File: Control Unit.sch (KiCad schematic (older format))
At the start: 0 parts

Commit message: made the CU , need to change the IR
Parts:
- added R8: 1K, Resistor_THT:R_Axial_DIN0204_L3.6mm_D1.6mm_P7.62mm_Horizontal, symbol 16bitCpu-rescue:R-Device
- added SW3: SW_Push-Switch, Button_Switch_THT:SW_PUSH-12mm, symbol 16bitCpu-rescue:SW_Push-Switch
- added U58: 7400, Package_DIP:DIP-14_W7.62mm, symbol 74xx:7400
- added U62: 74LS161-74xx, Package_DIP:DIP-16_W7.62mm, symbol 16bitCpu-rescue:74LS161-74xx
- added U63, U64, U65: AT28C64B-15PU, ROM:ZIF-AT28C64B-15PU, symbol AT28C64B-15PU:AT28C64B-15PU
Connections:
- net labels added: +5V-power, ALU_SU, CF, CLR, GND-power, PC_CE, RESET_COUNTER, VCC-power, ZF, ~ALU_EO, ~ALU_FI, ~CLR, ~IR_13AO, ~IR_AI, ~IR_AO, ~PC_CO, ~PC_J, ~R1_AI, ~R1_AO, ~R2_AI, ~R2_AO, ~RAM_AI, ~RAM_AO, ~RAM_MEMOE, ~RAM_MEMWE
- net labels removed: Bus0, Bus1, Bus10, Bus11, Bus12, Bus13, Bus14, Bus15, Bus2, Bus3, Bus4, Bus5, Bus6, Bus7, Bus8, Bus9
- wire segments 25 -> 165
- no-connect marks 0 -> 11

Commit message: non floating ram and ir , added stack register
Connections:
- net ~SI: now reaches U63.13 (I/O2)
- net ~SO: now reaches U63.15 (I/O3)
- no-connect marks 11 -> 9
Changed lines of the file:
@@
 $Descr A2 23386 16535
 encoding utf-8
-Sheet 9 9
+Sheet 9 10
 Title ""
 Date ""
@@
 Wire Wire Line
 	7100 7500 8400 7500
-Wire Wire Line
-	7100 7700 8400 7700
-Wire Wire Line
-	7100 7800 8400 7800
 Wire Wire Line
 	7100 7900 8400 7900
@@
 Text HLabel 8400 7500 2    50   Output ~ 0
 ~PC_CO
-NoConn ~ 8400 7700
-NoConn ~ 8400 7800
 NoConn ~ 8400 7900
 NoConn ~ 8400 8000
@@
 Wire Wire Line
 	7950 1950 7950 3900
+Wire Wire Line
+	7100 7700 9300 7700
+Text HLabel 9300 7700 2    50   Output ~ 0
+~SI
+Wire Wire Line
+	7100 7800 9200 7800
+Text HLabel 9200 7800 2    50   Output ~ 0
+~SO
 $EndSCHEMATC

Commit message: Added X register
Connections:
- net ~XI: now reaches U63.16 (I/O4)
- net ~XO: now reaches U63.17 (I/O5)
- no-connect marks 9 -> 7
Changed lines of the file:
@@
 $Descr A2 23386 16535
 encoding utf-8
-Sheet 9 10
+Sheet 9 11
 Title ""
 Date ""
@@
 Wire Wire Line
 	7100 7500 8400 7500
-Wire Wire Line
-	7100 7900 8400 7900
-Wire Wire Line
-	7100 8000 8400 8000
 Wire Wire Line
 	7100 8100 8400 8100
@@
 Text HLabel 8400 7500 2    50   Output ~ 0
 ~PC_CO
-NoConn ~ 8400 7900
-NoConn ~ 8400 8000
 NoConn ~ 8400 8100
 NoConn ~ 8400 8200
@@
 Text HLabel 9200 7800 2    50   Output ~ 0
 ~SO
+Text HLabel 10600 7900 2    50   Output ~ 0
+~XI
+Text HLabel 10500 8000 2    50   Output ~ 0
+~XO
+Wire Wire Line
+	7100 7900 10600 7900
+Wire Wire Line
+	7100 8000 10500 8000
 $EndSCHEMATC

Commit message: back to 13 bit addresses
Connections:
- net ~IR_13AO renamed ~IR_8O
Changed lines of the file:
@@
 ~IR_AO
 Text HLabel 8450 5750 2    50   Output ~ 0
-~IR_13AO
+~IR_8O
 Text HLabel 8450 5850 2    50   Output ~ 0
 ~PC_J

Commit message: Let there be light
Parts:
- added D100, D101, D102, D103, D104, D105, D106, D107, D108, D109, D110, D111, D112, D113, D114, D115, D116, D117, D118, D97, D98, D99: LED, LED_THT:LED_D3.0mm, symbol Device:LED
- added R105, R106, R107, R108, R109, R110, R111, R112, R113, R114, R115, R116, R117, R118, R119, R120, R121, R122, R123, R124, R125, R126: 220, Resistor_THT:R_Axial_DIN0204_L3.6mm_D1.6mm_P7.62mm_Horizontal, symbol Device:R
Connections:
- net ALU_SU: now also D98.2 (A)
- net GND: now also R105.2, R106.2, R107.2, R108.2, R109.2, R110.2, R111.2, R112.2, R113.2, R114.2, R115.2, R116.2, R117.2, R118.2, R119.2, R120.2, R121.2, R122.2, R123.2, R124.2, R125.2, R126.2
- net PC_CE: now also D112.2 (A)
- net RESET_COUNTER: now also D114.2 (A)
- net ~ALU_EO: now also D99.2 (A)
- net ~ALU_FI: now also D97.2 (A)
- net ~IR_8O: now also D110.2 (A)
- net ~IR_AI: now also D108.2 (A)
- net ~IR_AO: now also D109.2 (A)
- net ~PC_CO: now also D113.2 (A)
- net ~PC_J: now also D111.2 (A)
- net ~R1_AI: now also D100.2 (A)
- net ~R1_AO: now also D101.2 (A)
- net ~R2_AI: now also D102.2 (A)
- net ~R2_AO: now also D103.2 (A)
- net ~RAM_AI: now also D104.2 (A)
- net ~RAM_AO: now also D105.2 (A)
- net ~RAM_MEMOE: now also D106.2 (A)
- net ~RAM_MEMWE: now also D107.2 (A)
- net ~SI: now also D115.2 (A)
- net ~SO: now also D116.2 (A)
- net ~XI: now also D117.2 (A)
- net ~XO: now also D118.2 (A)
- new net: D112.1 (K), R120.1
- new net: D111.1 (K), R119.1
- new net: D110.1 (K), R118.1
- new net: D109.1 (K), R117.1
- new net: D108.1 (K), R116.1
- new net: D107.1 (K), R115.1
- new net: D106.1 (K), R114.1
- new net: D105.1 (K), R113.1
- new net: D104.1 (K), R112.1
- new net: D103.1 (K), R111.1
- new net: D102.1 (K), R110.1
- new net: D101.1 (K), R109.1
- new net: D100.1 (K), R108.1
- new net: D99.1 (K), R107.1
- new net: D98.1 (K), R106.1
- new net: D97.1 (K), R105.1
- new net: D118.1 (K), R126.1
- new net: D117.1 (K), R125.1
- new net: D116.1 (K), R124.1
- new net: D115.1 (K), R123.1
- new net: D114.1 (K), R122.1
- new net: D113.1 (K), R121.1

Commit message: Added NAND GATES in ALU
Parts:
- renumbered D97 to D49, D98 to D50, D99 to D51, D100 to D52, D101 to D53, D102 to D54, D103 to D55, D104 to D56, D105 to D57, D106 to D58, D107 to D59, D108 to D60, D109 to D61, D110 to D62, D111 to D63, D112 to D64, D113 to D65, D114 to D66, D115 to D67, D116 to D68, D117 to D69, D118 to D70, R8 to R49, R105 to R50, R106 to R51, R107 to R52, R108 to R53, R109 to R54, R110 to R55, R111 to R56, R112 to R57, R113 to R58, R114 to R59, R115 to R60, R116 to R61, R117 to R62, R118 to R63, R119 to R64, R120 to R65, R121 to R66, R122 to R67, R123 to R68, R124 to R69, R125 to R70, R126 to R71, SW3 to SW1, U58 to U19, U62 to U20, U63 to U21, U64 to U22, U65 to U23

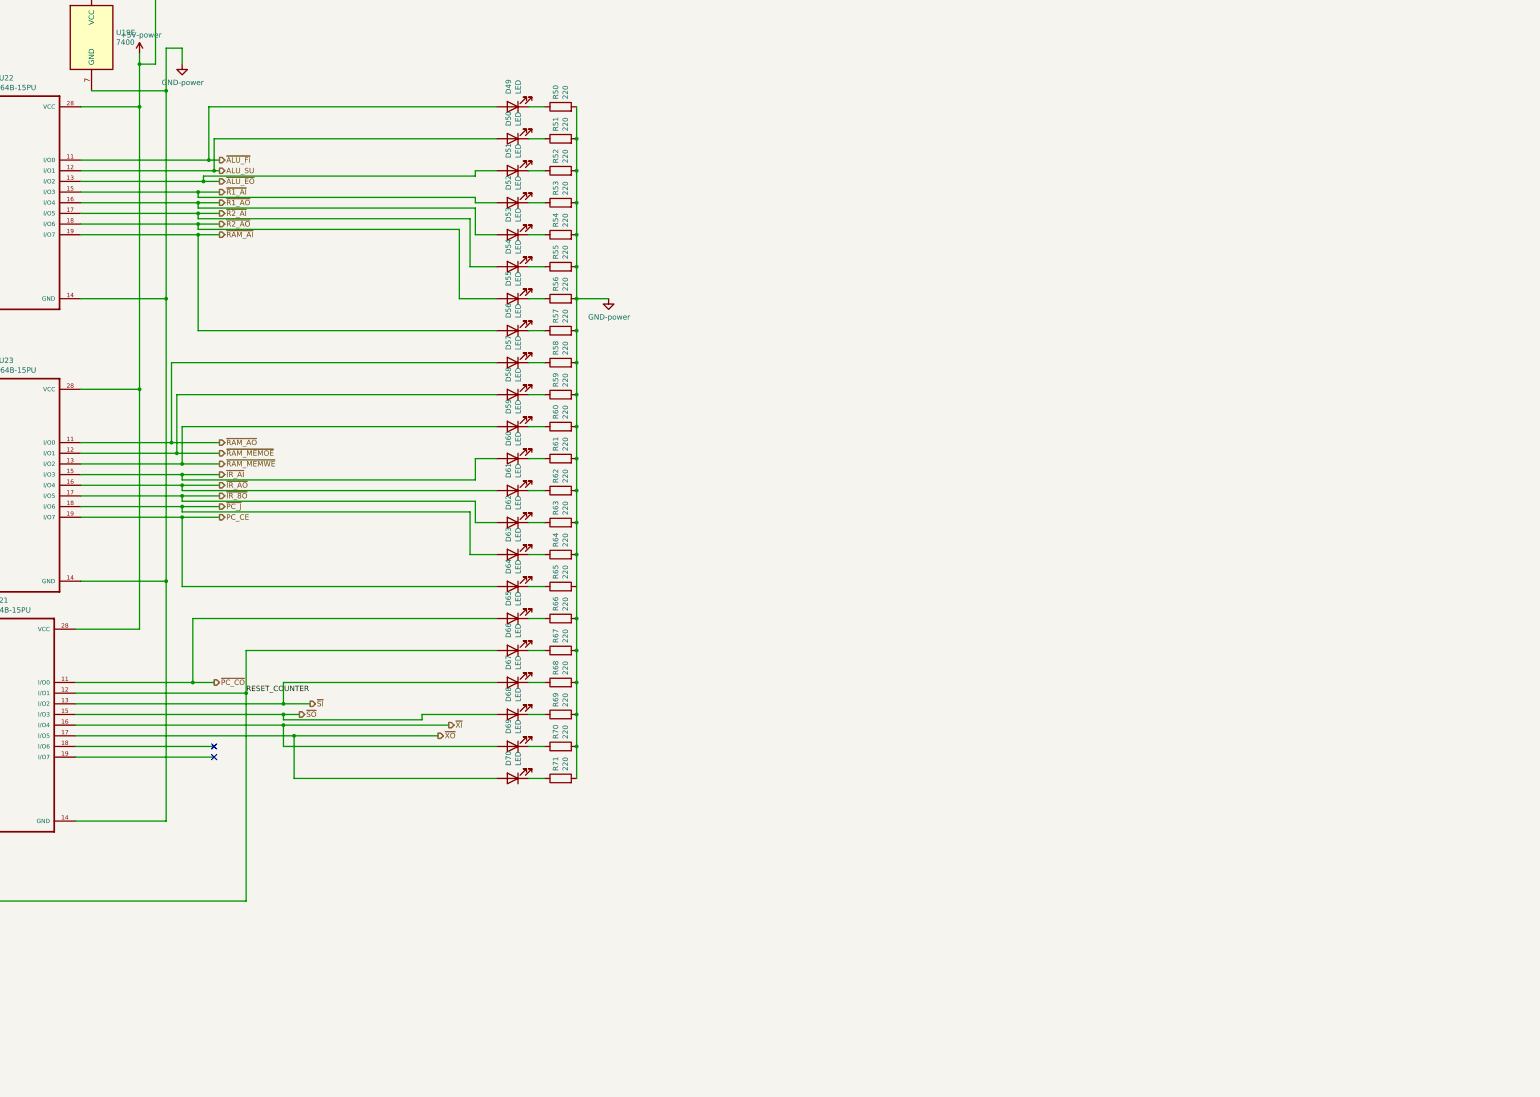
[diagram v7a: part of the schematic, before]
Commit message: added 3-8 decoders to cu
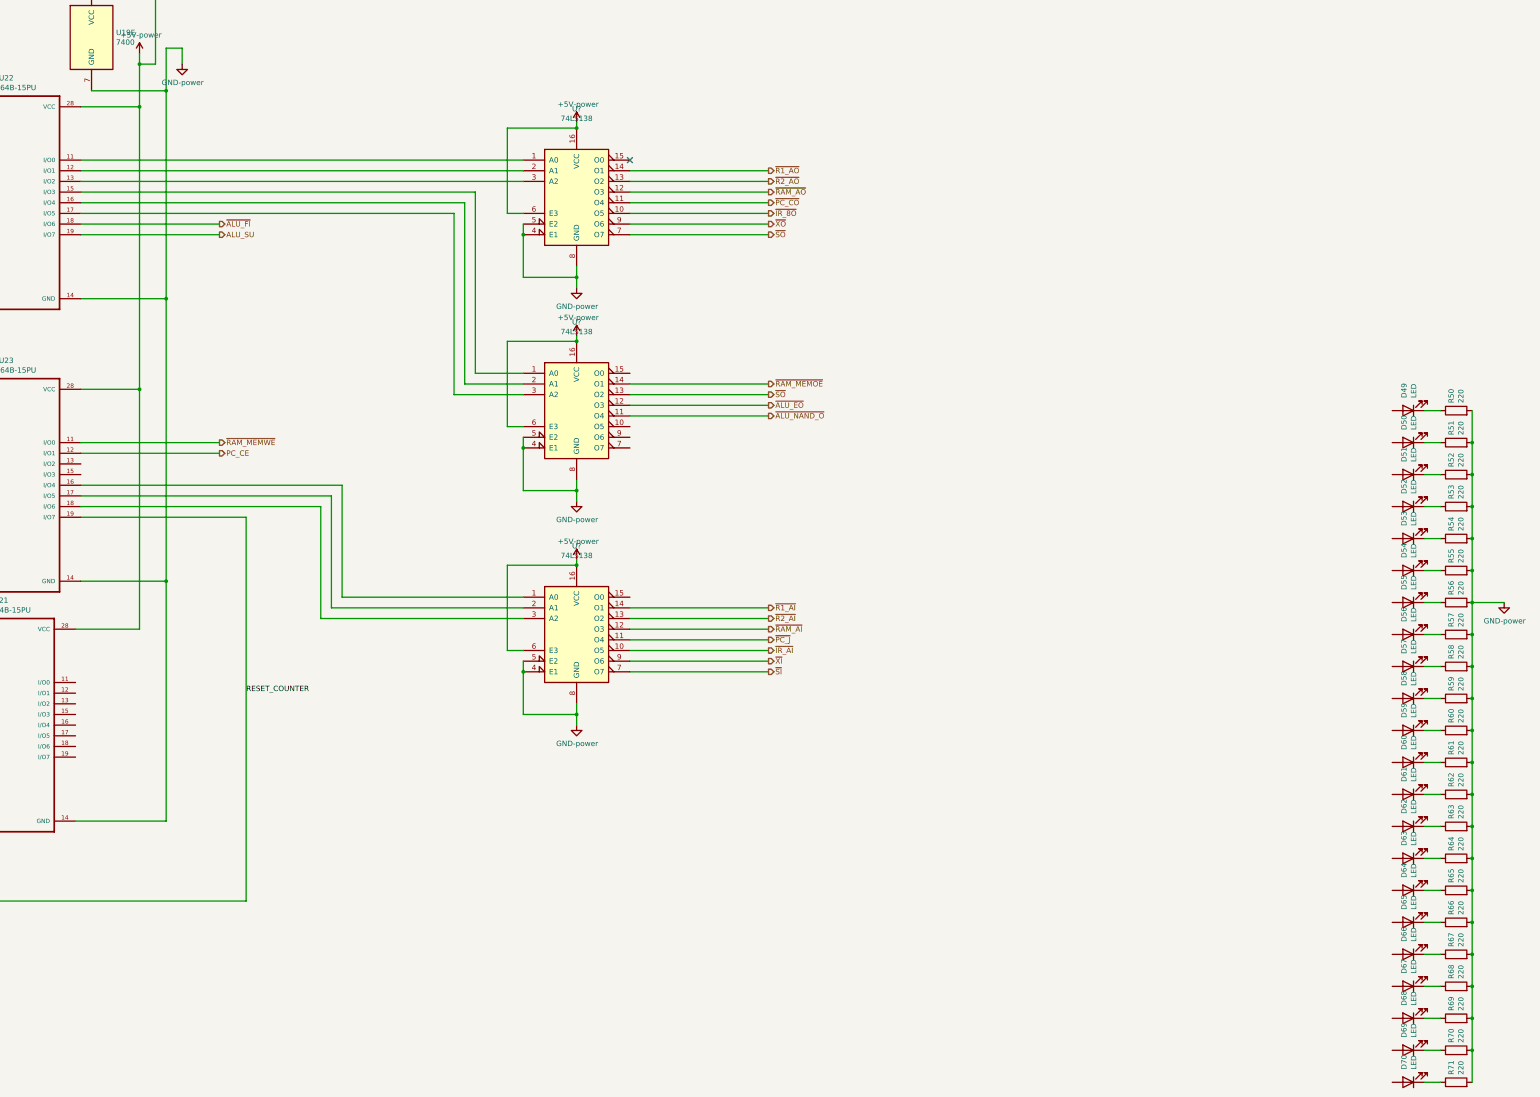
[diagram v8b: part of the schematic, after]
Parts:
- added U? (x3): 74LS138, symbol 74xx:74LS138
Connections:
- net +5V: now also U?.16 (VCC), U?.16 (VCC), U?.16 (VCC), U?.6 (E3), U?.6 (E3), U?.6 (E3)
- net ALU_SU: now also U22.19 (I/O7); no longer D50.2 (A), U22.12 (I/O1)
- net GND: now also U?.4 (E1), U?.4 (E1), U?.4 (E1), U?.5 (E2), U?.5 (E2), U?.5 (E2), U?.8 (GND), U?.8 (GND), U?.8 (GND)
- net PC_CE: now also U23.12 (I/O1); no longer D64.2 (A), U23.19 (I/O7)
- net RESET_COUNTER: now also U23.19 (I/O7); no longer D66.2 (A), U21.12 (I/O1)
- net ~ALU_EO: now also U?.12 (O3); no longer D51.2 (A), U22.13 (I/O2)
- net ~ALU_FI: now also U22.18 (I/O6); no longer D49.2 (A), U22.11 (I/O0)
- net ~IR_8O: now also U?.10 (O5); no longer D62.2 (A), U23.17 (I/O5)
- net ~IR_AI: now also U?.10 (O5); no longer D60.2 (A), U23.15 (I/O3)
- net ~PC_CO: now also U?.11 (O4); no longer D65.2 (A), U21.11 (I/O0)
- net ~PC_J: now also U?.11 (O4); no longer D63.2 (A), U23.18 (I/O6)
- net ~R1_AI: now also U?.14 (O1); no longer D52.2 (A), U22.15 (I/O3)
- net ~R1_AO: now also U?.14 (O1); no longer D53.2 (A), U22.16 (I/O4)
- net ~R2_AI: now also U?.13 (O2); no longer D54.2 (A), U22.17 (I/O5)
- net ~R2_AO: now also U?.13 (O2); no longer D55.2 (A), U22.18 (I/O6)
- net ~RAM_AI: now also U?.12 (O3); no longer D56.2 (A), U22.19 (I/O7)
- net ~RAM_AO: now also U?.12 (O3); no longer D57.2 (A), U23.11 (I/O0)
- net ~RAM_MEMOE: now also U?.14 (O1); no longer D58.2 (A), U23.12 (I/O1)
- net ~RAM_MEMWE: now also U23.11 (I/O0); no longer D59.2 (A), U23.13 (I/O2)
- net ~SI: now also U?.7 (O7); no longer D67.2 (A), U21.13 (I/O2)
- net ~SO: now also U?.13 (O2), U?.7 (O7); no longer D68.2 (A), U21.15 (I/O3)
- net ~XI: now also U?.9 (O6); no longer D69.2 (A), U21.16 (I/O4)
- net ~XO: now also U?.9 (O6); no longer D70.2 (A), U21.17 (I/O5)
- net ~IR_AO: no longer names the net of U23.16 (I/O4)
- net ~IR_AO: now also U?.1 (A0); no longer D61.2 (A)
- new net: U22.11 (I/O0), U?.1 (A0)
- new net: U22.12 (I/O1), U?.2 (A1)
- new net: U22.13 (I/O2), U?.3 (A2)
- new net: U22.15 (I/O3), U?.1 (A0)
- new net: U22.16 (I/O4), U?.2 (A1)
- new net: U22.17 (I/O5), U?.3 (A2)
- new net: U23.17 (I/O5), U?.2 (A1)
- new net: U23.18 (I/O6), U?.3 (A2)
- new net ~ALU_NAND_O: U?.11 (O4)
- no-connect marks 7 -> 6
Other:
- moved on the sheet: D49, D50, D51, D52, D53, D54, D55, D56, D57, D58, D59, D60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
